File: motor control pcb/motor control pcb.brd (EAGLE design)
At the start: 73.2 x 73.9 mm, 85 parts, among them IC1 7805TV, IC2 A3949, IC3 SMS-12, IC4 SN75176ASOIC, IC5 ATMEGA328, IC6 FT232RL, IC7 LM358D, IC8 MAX6675, Q1 PH7030L, Q2 PH7030L, Q3 PH7030L, Q4 16MHZ, T1 BSS84, X1 9090-4V, X5 C-GRID-04-70543, X6 MSTBV10

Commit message: Motor control PCB
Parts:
- removed 12V, 5V, A, B, C, DIR1, RX, TX: (no value), SparkFun:LED-0805
- removed C1, C2: 100uF, rcl:E3,5-8
- removed C10, C11, C16, C17, C18, C19, C3, C4, C5, C6: 100nF, SparkFun:0805
- removed C9: .22uF, SparkFun:0805
- removed IC1: 7805TV, linear:TO220V
- removed IC2: A3949, reprap:SO16W
- removed IC3: SMS-12, reprap:SOT23-6
- removed IC6: FT232RL, reprap:SMARTPRJ_SSOP28
- removed IC7: LM358D, linear:SO08
- removed IC8: MAX6675, reprap:SO08
- removed JP4: (no value), pinhead:1X04
- removed JP6, JP7: (no value), pinhead:2X03
- removed L1: 100mA, resistor:L1812
- removed Q1, Q2, Q3: PH7030L, transistor-power:SOT669
- removed R10, R20, R21, R5, R6: 4.7K, SparkFun:0805
- removed R11, R13, R14, R15, R17, R18, R19, R22, R29, R31: 1K, SparkFun:0805
- removed R12, R4: 10K, SparkFun:0805
- removed R9: 2.2K, SparkFun:0805
- removed SPEED1: 1, SparkFun:LED-0805
- removed T1: BSS84, zetex:SOT-23
- removed TP3, TP4: PTR1TP09R, testpad:TP09R
- removed U$1, U$2, U$3, U$4: (no value), holes:3,0
- removed X2: (no value), reprap:SMARTPRJ_PN61729
- removed X5: C-GRID-04-70543, reprap:70543-04
- removed X6: MSTBV10, con-phoenix-508:MSTBV10
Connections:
- removed net APWR: A.C, Q3.MB, X6.8
- removed net BPWR: B.C, Q1.MB, X6.6
- removed net CPWR: C.C, Q2.MB, X6.4
- removed net N$1: C5.2, IC8.1, IC8.2, X6.9
- removed net N$11: C5.1, IC8.3, X6.10
- removed net N$12: IC2.5, R4.2
- removed net N$18: R11.1, SPEED1.C
- removed net N$2: C.A, R14.1
- removed net N$23: DIR1.C, R13.2
- removed net N$25: 5V.A, R15.1
- removed net N$26: 12V.A, R9.1
- removed net N$29: IC6.15, X2.3
- removed net N$3: C9.2, IC2.15
- removed net N$30: IC6.16, X2.2
- removed net N$36: C18.1, IC6.19
- removed net N$37: L1.2, X2.1
- removed net N$38: C16.2, IC6.17
- removed net N$39: R19.2, RX.A
- removed net N$4: IC2.7, IC3.6, X6.1
- removed net N$40: R22.2, TX.A
- removed net N$41: A.A, R31.1
- removed net N$42: B.A, R29.1
- removed net N$44: IC6.23, RX.C
- removed net N$45: IC6.22, TX.C
- removed net N$46: C19.1, IC6.2
- removed net N$47: IC6.1, R17.2
- removed net N$48: IC6.5, R18.2
- removed net N$5: IC2.10, IC3.4, X6.2
- removed net N$50: IC7.1, IC7.5
- removed net N$51: IC7.6, IC7.7, T1.3
- removed net N$6: C10.2, IC2.12
- removed net N$7: C10.1, IC2.11
- removed net N$9: C11.1, IC2.14
- removed net USBVCC: C17.2, IC6.20, IC6.4, IC7.2, L1.1, R19.1, R22.1, T1.1, TP3.TP
- removed net V+: IC7.8
- removed net V-: IC7.4
- net +12V: no longer C1.+, C11.2, C3.1, IC1.1, IC2.9, IC7.3, R14.2, R29.2, R31.2, R9.2, X6.3, X6.5, X6.7
- net A2: no longer JP6.6
- net A3: no longer JP6.5
- net A6: no longer JP7.6
- net A7: no longer JP7.5
- net D10: no longer Q3.4, R5.2
- net D12: no longer IC8.7
- net D13: no longer IC8.5
- net D2: no longer X5.3
- net D3: no longer X5.4
- net D4: no longer IC8.6, R12.1
- net D5: no longer IC2.6, SPEED1.A
- net D6: no longer Q2.4, R10.2
- net D8: no longer DIR1.A, IC2.3
- net D9: no longer Q1.4, R6.2
- net GND: no longer 12V.C, 5V.C, C1.-, C16.1, C17.1, C18.2, C2.-, C3.2, C4.2, C6.1, C9.1, IC1.2, IC2.13, IC2.2, IC2.4, IC2.8, IC3.2, IC3.5, IC6.18, IC6.21, IC6.25, IC6.26, IC6.7, JP4.2, JP6.1, JP6.2, JP7.1, JP7.2, Q1.1, Q1.2, Q1.3, Q2.1, Q2.2, Q2.3, Q3.1, Q3.2, Q3.3, R10.1, R11.2, R13.1, R5.1, R6.1, X2.4, X2.P$1, X2.P$2, X5.2
- net RESET: no longer C19.2
- net RX: no longer R17.1
- net SCL: no longer JP4.4, R21.1
- net SDA: no longer JP4.3, R20.1
- net TX: no longer R18.1
- net VCC: no longer C2.+, C4.1, C6.2, IC1.3, IC8.4, JP4.1, JP6.3, JP6.4, JP7.3, JP7.4, R12.2, R15.2, R20.2, R21.2, R4.1, T1.2, TP4.TP, X5.1
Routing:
- net VCC: track 229.2 -> 0.00 mm, vias 4 -> 0
- net +12V: track 190.0 -> 0.00 mm, vias 6 -> 0
- net RESET: track 93.1 -> 0.00 mm, vias 1 -> 0
- net GND: track 84.8 -> 0.00 mm, vias 10 -> 0
- net D4: track 75.4 -> 0.00 mm, vias 2 -> 0
- net D13: track 66.0 -> 0.00 mm, vias 3 -> 0
- net USBVCC: track 61.5 -> 0.00 mm, vias 2 -> 0
- net TX: track 61.0 -> 0.00 mm, vias 3 -> 0
- net D12: track 54.9 -> 0.00 mm, vias 2 -> 0
- net RX: track 44.4 -> 0.00 mm, vias 3 -> 0
- net D8: track 36.4 -> 0.00 mm
- net D5: track 34.4 -> 0.00 mm, vias 2 -> 0
- net N$42: track 32.0 -> 0.00 mm, vias 2 -> 0
- net D10: track 31.5 -> 0.00 mm, vias 2 -> 0
- net SDA: track 28.0 -> 0.00 mm, vias 2 -> 0
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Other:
- board text removed: "+"
- board text removed: "15"
- board text removed: "17"
- board text removed: "1A"
- board text removed: "1B"
- board text removed: "25"
- board text removed: "5V"
- board text removed: "9"
- board text removed: "A2"
- board text removed: "A3"
- board text removed: "A6"
- board text removed: "A7"
- board text removed: "BASSDRIVE.COM"
- board text removed: "Big ups Arduino."
- board text removed: "Bre3po"
- board text removed: "Catarina"
- board text removed: "Controller"
- board text removed: "D"
- board text removed: "Docs: wiki.makerbot.com/ec3"
- board text removed: "EXTRA"
- board text removed: "Extruder"
- board text removed: "FAN"
- board text removed: "G"
- board text removed: "GND"
- board text removed: "H. Mulliken"
- board text removed: "HEATER"
- board text removed: "Hoeken"
- board text removed: "KEEP IT LOCKED"
- board text removed: "Marisol"
- board text removed: "NYC Resistor"
- board text removed: "Paxotron"
- board text removed: "Phooky"
- board text removed: "QUADRATURE"
- board text removed: "SCL"
- board text removed: "SDA"
- board text removed: "Scribel"
- board text removed: "Shouts to:"
- board text removed: "T+"
- board text removed: "T-"
- board text removed: "THERMOCOUPLE"
- board text removed: "Widget"
- board text removed: "v3.6"

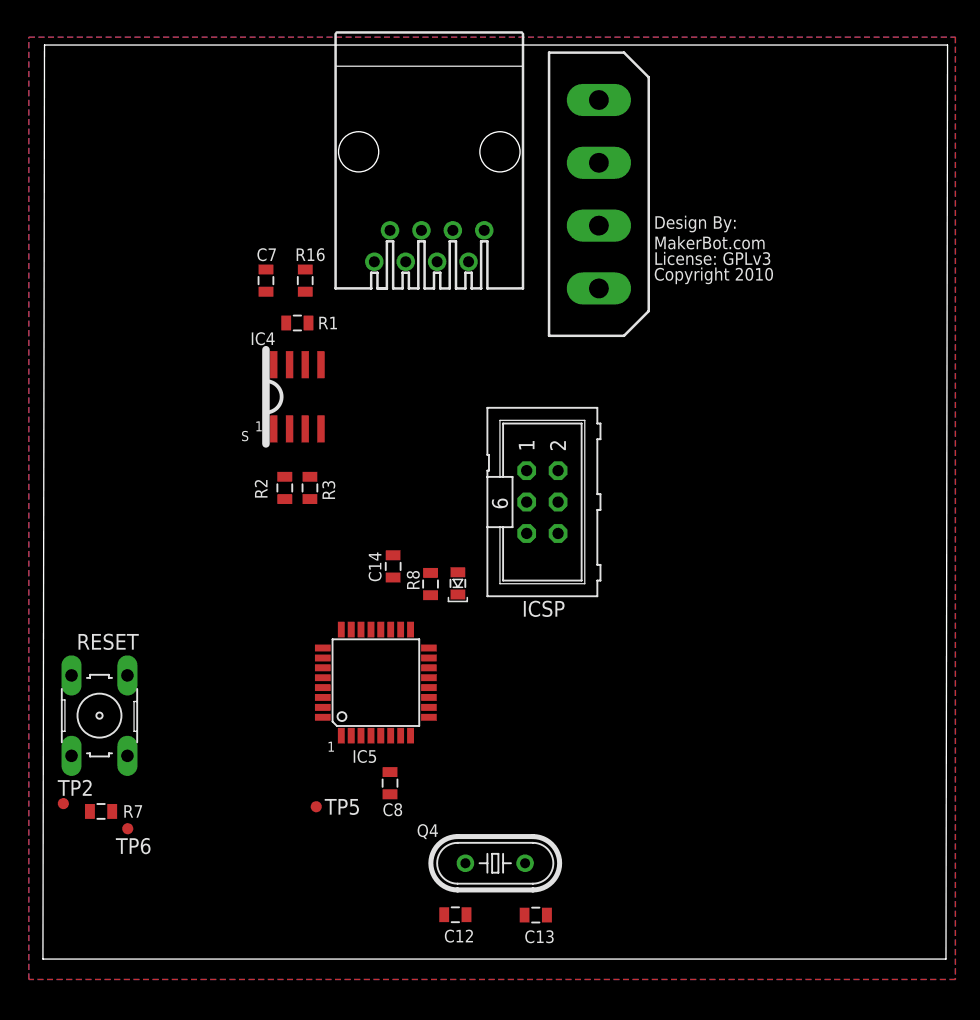
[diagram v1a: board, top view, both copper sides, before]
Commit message: Rev 0 of the motor control pcb; update for smaller traces.
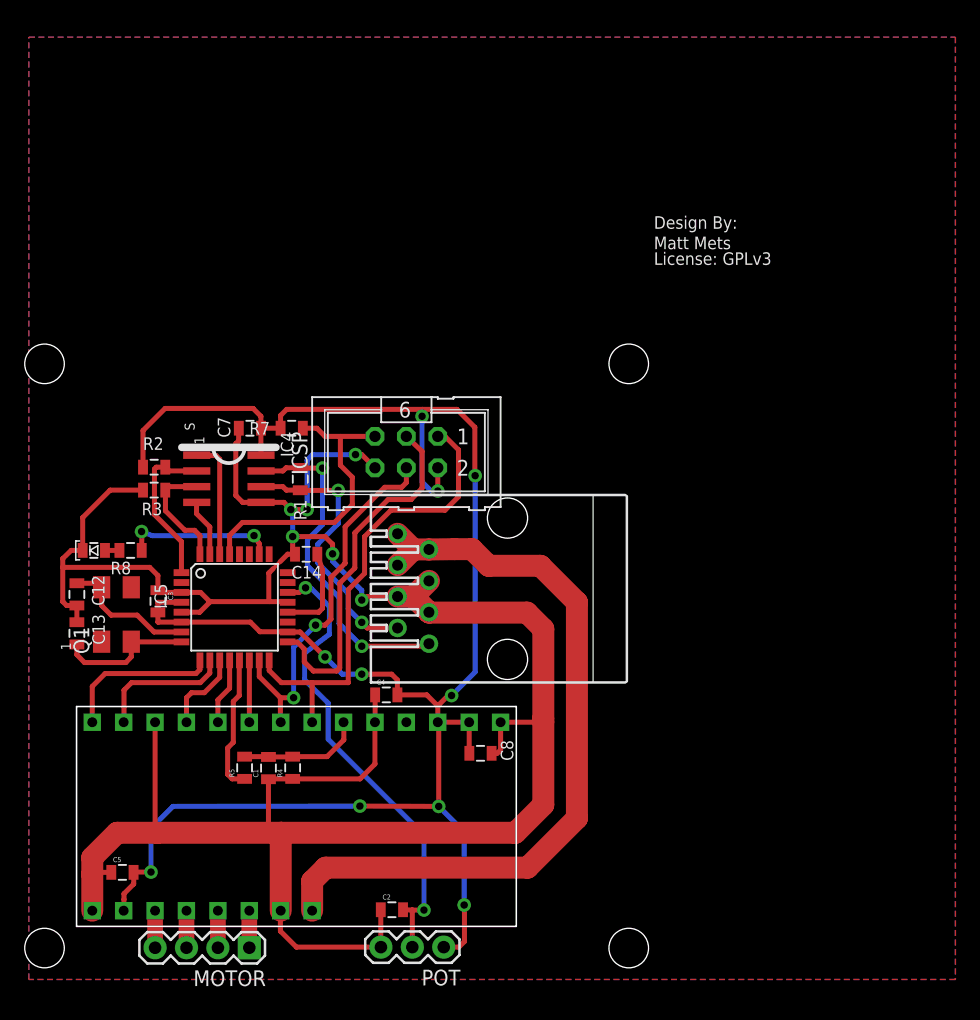
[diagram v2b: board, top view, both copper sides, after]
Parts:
- removed Q4: 16MHZ, crystal:HC49/S
- removed R16: 180, SparkFun:0805
- removed RESET: (no value), switch-omron:B3F-10XX
- removed TP2, TP5, TP6: PTR1TP09R, testpad:TP09R
- removed X1: 9090-4V, con-thomas-betts:9090-4V
- added C1, C2: 16pf, SparkFun:0805
- added C3, C4, C5: 100nF, SparkFun:0805
- added MOTOR: (no value), SparkFun:1X04
- added POT: (no value), SparkFun:1X03
- added Q1: (no value), blinkyboard:GLOWBOARD_ABMM2_CRYSTAL
- added R4: 1K, SparkFun:0805
- added R5: 4.7k, SparkFun:0805
- added U$1: POLOLU_DRIVER, sonos_library:POLOLU_DRIVER
- moved C13 43.5 mm to (2.62, 25.5), turned to 270 degrees
- moved C12 40.1 mm to (2.62, 28.6), turned to 90 degrees
- moved J1 35.9 mm to (37.4, 29.1), turned to 90 degrees
- moved R7 34.6 mm to (20.0, 42.0), turned to 180 degrees
- moved DEBUG 29.6 mm to (3.99, 32.2), turned to 90 degrees
- moved R8 24.4 mm to (6.96, 32.2), turned to 0 degrees
- moved IC5 13.0 mm to (15.4, 27.6), turned to 0 degrees
- moved R1 12.6 mm to (20.7, 37.9), turned to 90 degrees
- moved R3 12.6 mm to (8.86, 37.0), turned to 180 degrees
- moved C7 12.0 mm to (16.6, 42.0), turned to 0 degrees
- moved ICSP 11.7 mm to (29.3, 40.1), turned to 180 degrees
- moved R2 10.7 mm to (8.86, 38.9), turned to 180 degrees
- moved IC4 8.64 mm to (14.9, 37.9), turned to 270 degrees
- moved C8 7.70 mm to (35.3, 15.7), turned to 180 degrees
- moved C14 7.11 mm to (21.2, 31.9), turned to 0 degrees
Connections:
- removed net +12V: X1.4
- removed net N$32: C13.2, IC5.8, Q4.1
- removed net N$83: J1.6, J1.7, J1.8, R16.2
- new net N$11: C1.2, R4.2, R5.2, U$1.REF
- new net N$2: MOTOR.1, U$1.2B
- new net N$3: MOTOR.2, U$1.2A
- new net N$4: MOTOR.3, U$1.1A
- new net N$5: MOTOR.4, U$1.1B
- new net N$6: C13.2, IC5.8, Q1.P$1
- new net VMOT: J1.6, J1.7, J1.8, U$1.VMOT
- net A0: no longer IC4.3, R3.1
- net A1: no longer IC4.2, R2.1
- net A3: now also R8.2
- net A7: now also C2.2, POT.2
- net D10: now also U$1.MS2
- net D11: now also U$1.MS1
- net D12: now also U$1./EN
- net D13: no longer R8.2
- net D2: now also IC4.3, R3.1
- net D3: now also IC4.2, R2.1
- net D5: now also U$1.DIR
- net D6: now also U$1.STEP
- net D7: now also U$1./RST
- net D8: now also U$1.MS3
- net D9: now also R5.1
- net GND: now also C1.1, C2.1, C3.1, C4.1, C5.1, J1.3, J1.4, J1.5, POT.3, R4.1, U$1./SLP, U$1.GND, U$1.GND1, U$1.GND2, U$1.GND3; no longer R16.1, RESET.3, RESET.4, X1.2, X1.3
- net N$31: now also Q1.P$3; no longer Q4.2
- net RESET: no longer RESET.1, RESET.2, TP2.TP
- net SCL: no longer TP5.TP
- net SDA: no longer TP6.TP
- net VCC: now also C3.2, C4.2, C5.2, POT.1, U$1.5V, U$1.VDD, U$1.VDD1
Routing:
- net GND: track 0.00 -> 210.3 mm, vias 0 -> 6
- net VCC: track 0.00 -> 158.1 mm, vias 0 -> 10
- net VMOT: track 0.00 -> 62.0 mm
- net A7: track 0.00 -> 38.3 mm, vias 0 -> 2
- net D12: track 0.00 -> 38.0 mm
- net D11: track 0.00 -> 30.4 mm, vias 0 -> 2
- net D13: track 0.00 -> 29.0 mm
- net RS485B: track 0.00 -> 27.3 mm, vias 0 -> 2
- net RESET: track 0.00 -> 24.5 mm
- net RS485A: track 0.00 -> 22.5 mm, vias 0 -> 2
- net D5: track 0.00 -> 12.9 mm
- net D3: track 0.00 -> 12.9 mm
- net A3: track 0.00 -> 12.3 mm, vias 0 -> 2
- net N$31: track 0.00 -> 11.3 mm
- net D6: track 0.00 -> 11.1 mm
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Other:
- board size 73.2 x 73.9 mm -> 35.6 x 17.8 mm
- board text added: "Matt Mets"
- board text removed: "Copyright 2010"
- board text removed: "MakerBot.com"
